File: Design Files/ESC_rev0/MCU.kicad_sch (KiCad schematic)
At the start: 36 parts, among them J1 Conn_01x08, J2 Conn_01x06, J3 Conn_01x03, SW1 SW_DIP_x01, U4 STM32F405RGTx, Y1 Crystal

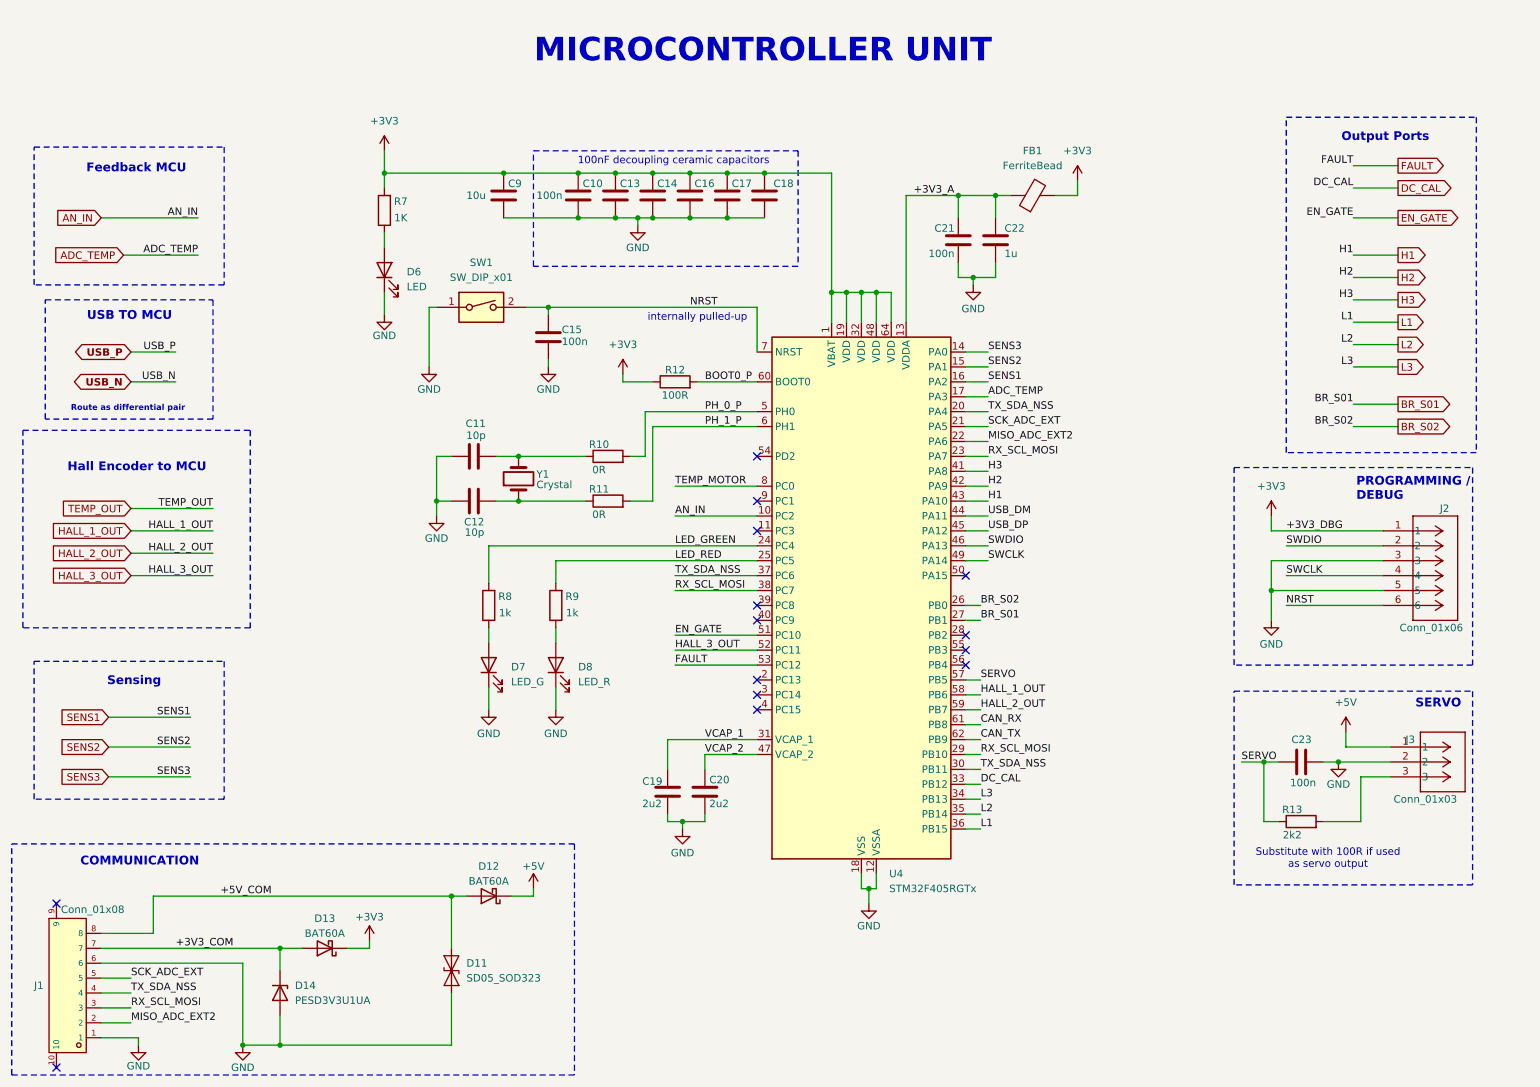
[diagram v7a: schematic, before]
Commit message: update 16
All components placed on board. Some components modifications and addition were made: added 3D models, changed some symbols and footprints positions and some component types.
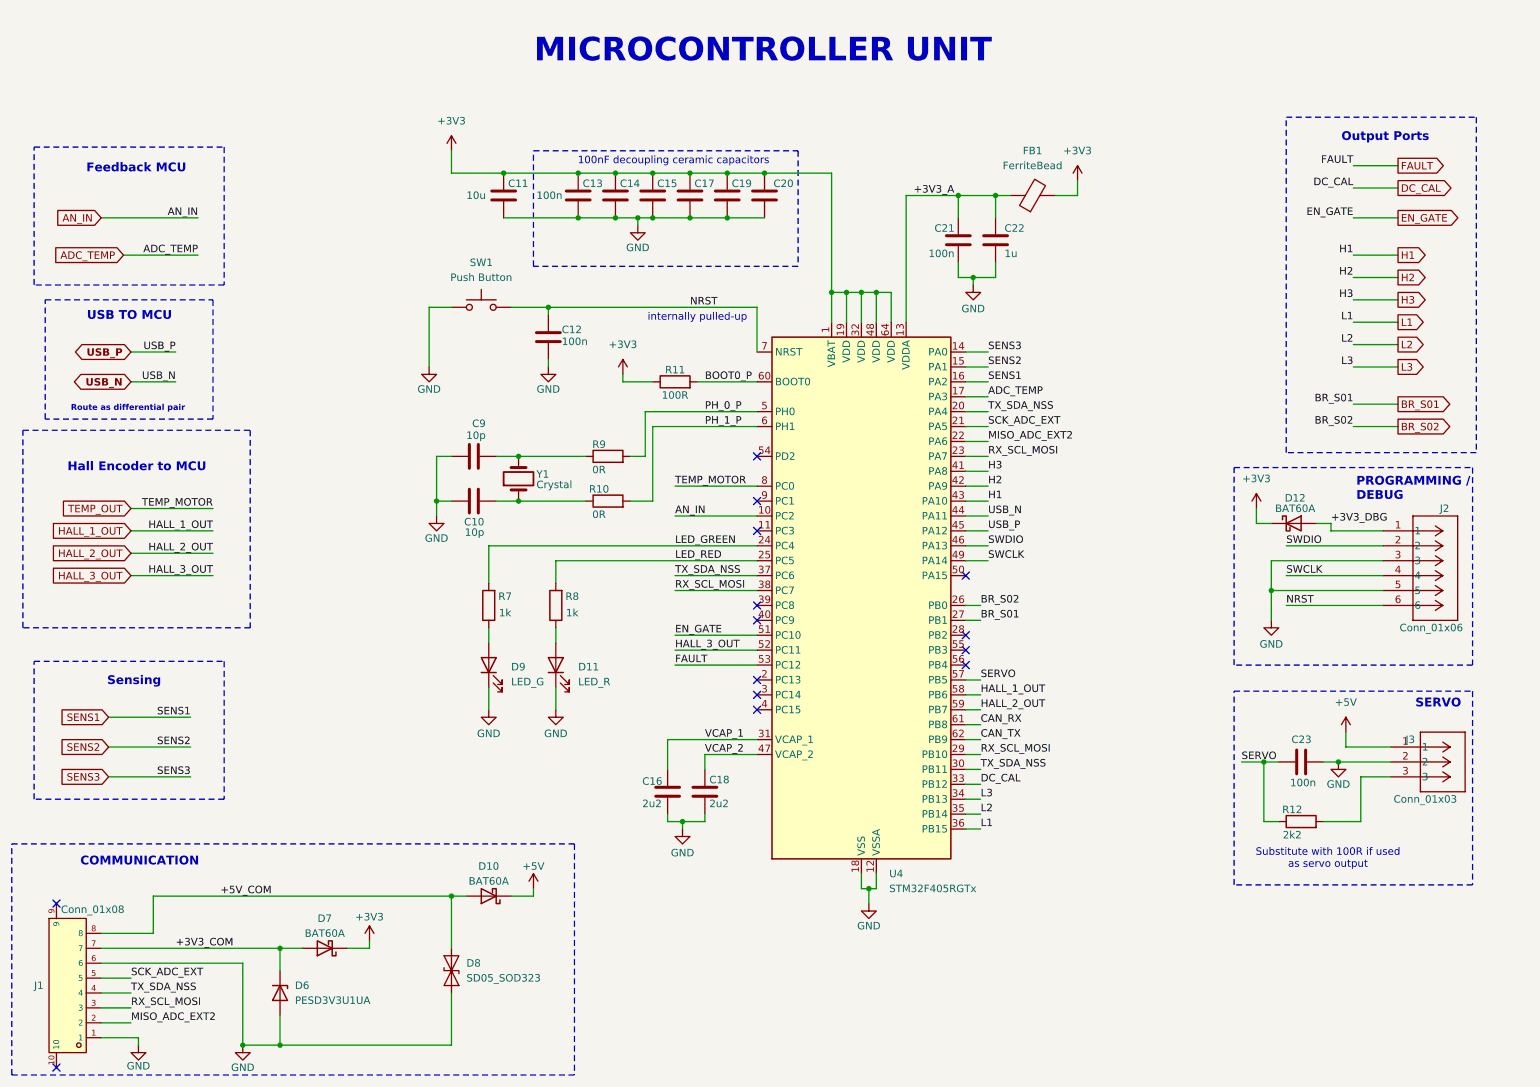
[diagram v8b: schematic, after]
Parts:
- removed D6: LED, LED_SMD:LED_0201_0603Metric, symbol Device:LED
- removed R7: 1K, Resistor_SMD:R_0603_1608Metric, symbol Device:R
- added D12: BAT60A, Diode_SMD:D_SOD-323, symbol Diode:BAT60A
- C10: renamed from C12; footprint Capacitor_SMD:C_0201_0603Metric -> Capacitor_SMD:C_0402_1005Metric
- C11: renamed from C9; footprint Capacitor_SMD:C_0201_0603Metric -> Capacitor_SMD:C_0603_1608Metric
- C12: renamed from C15; footprint Capacitor_SMD:C_0201_0603Metric -> Capacitor_SMD:C_0603_1608Metric
- C13: renamed from C10; footprint Capacitor_SMD:C_0201_0603Metric -> Capacitor_SMD:C_0603_1608Metric
- C14: renamed from C13; footprint Capacitor_SMD:C_0201_0603Metric -> Capacitor_SMD:C_0603_1608Metric
- C15: renamed from C14; footprint Capacitor_SMD:C_0201_0603Metric -> Capacitor_SMD:C_0603_1608Metric
- C16: renamed from C19; footprint Capacitor_SMD:C_0201_0603Metric -> Capacitor_SMD:C_0603_1608Metric
- C17: renamed from C16; footprint Capacitor_SMD:C_0201_0603Metric -> Capacitor_SMD:C_0603_1608Metric
- C18: renamed from C20; footprint Capacitor_SMD:C_0201_0603Metric -> Capacitor_SMD:C_0603_1608Metric
- C19: renamed from C17; footprint Capacitor_SMD:C_0201_0603Metric -> Capacitor_SMD:C_0603_1608Metric
- C20: renamed from C18; footprint Capacitor_SMD:C_0201_0603Metric -> Capacitor_SMD:C_0603_1608Metric
- C21, C22, C23: footprint Capacitor_SMD:C_0201_0603Metric -> Capacitor_SMD:C_0603_1608Metric
- C9: renamed from C11; footprint Capacitor_SMD:C_0201_0603Metric -> Capacitor_SMD:C_0402_1005Metric
- FB1: footprint Ferrite_THT:LairdTech_28C0236-0JW-10 -> Inductor_SMD:L_0805_2012Metric
- J2: footprint CONN_S6B-XH-SM4-TB_JST -> S6B-XH-SM4-TB:CONN_S6B-XH-SM4-TB_JST
- J3: footprint CONN3_S3B-XH_JST -> S3B-XH-SM4-TB:CONN3_S3B-XH_JST
- SW1: value SW_DIP_x01 -> Push Button; footprint Button_Switch_SMD:SW_DIP_SPSTx01_Slide_6.7x4.1mm_W6.73mm_P2.54mm_LowProfile_JPin -> Pushbutton 2p:SW_PTS636_SM43J_SMTR_LFS; symbol Switch:SW_DIP_x01 -> Switch:SW_Push
- Y1: footprint Crystal:Crystal_SMD_0603-4Pin_6.0x3.5mm_HandSoldering -> Crystal:Crystal_SMD_2520-4Pin_2.5x2.0mm
- renumbered D12 to D10, D8 to D11, D14 to D6, D13 to D7, D11 to D8, D7 to D9, R11 to R10, R12 to R11, R13 to R12, R8 to R7, R9 to R8, R10 to R9
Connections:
- net TEMP_MOTOR is gone; now on net TEMP_OUT: U4.8 (PC0)
- net USB_DM is gone; now on net USB_N: U4.44 (PA11)
- net USB_DP is gone; now on net USB_P: U4.45 (PA12)
- net +3V3: now also D12.1 (K); no longer J2.1
- new net +3V3_DBG: D12.2 (A), J2.1
